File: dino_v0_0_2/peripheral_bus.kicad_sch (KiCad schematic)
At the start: 9 parts, among them J1 DINO_BUS_SOCKET, J2 DINO_BUS_SOCKET, J3 DINO_BUS_SOCKET, J4 DINO_BUS_SOCKET, J5 DINO_BUS_SOCKET, J6 DINO_BUS_SOCKET, J7 DINO_BUS_SOCKET, J8 DINO_BUS_SOCKET, U78 74LS04

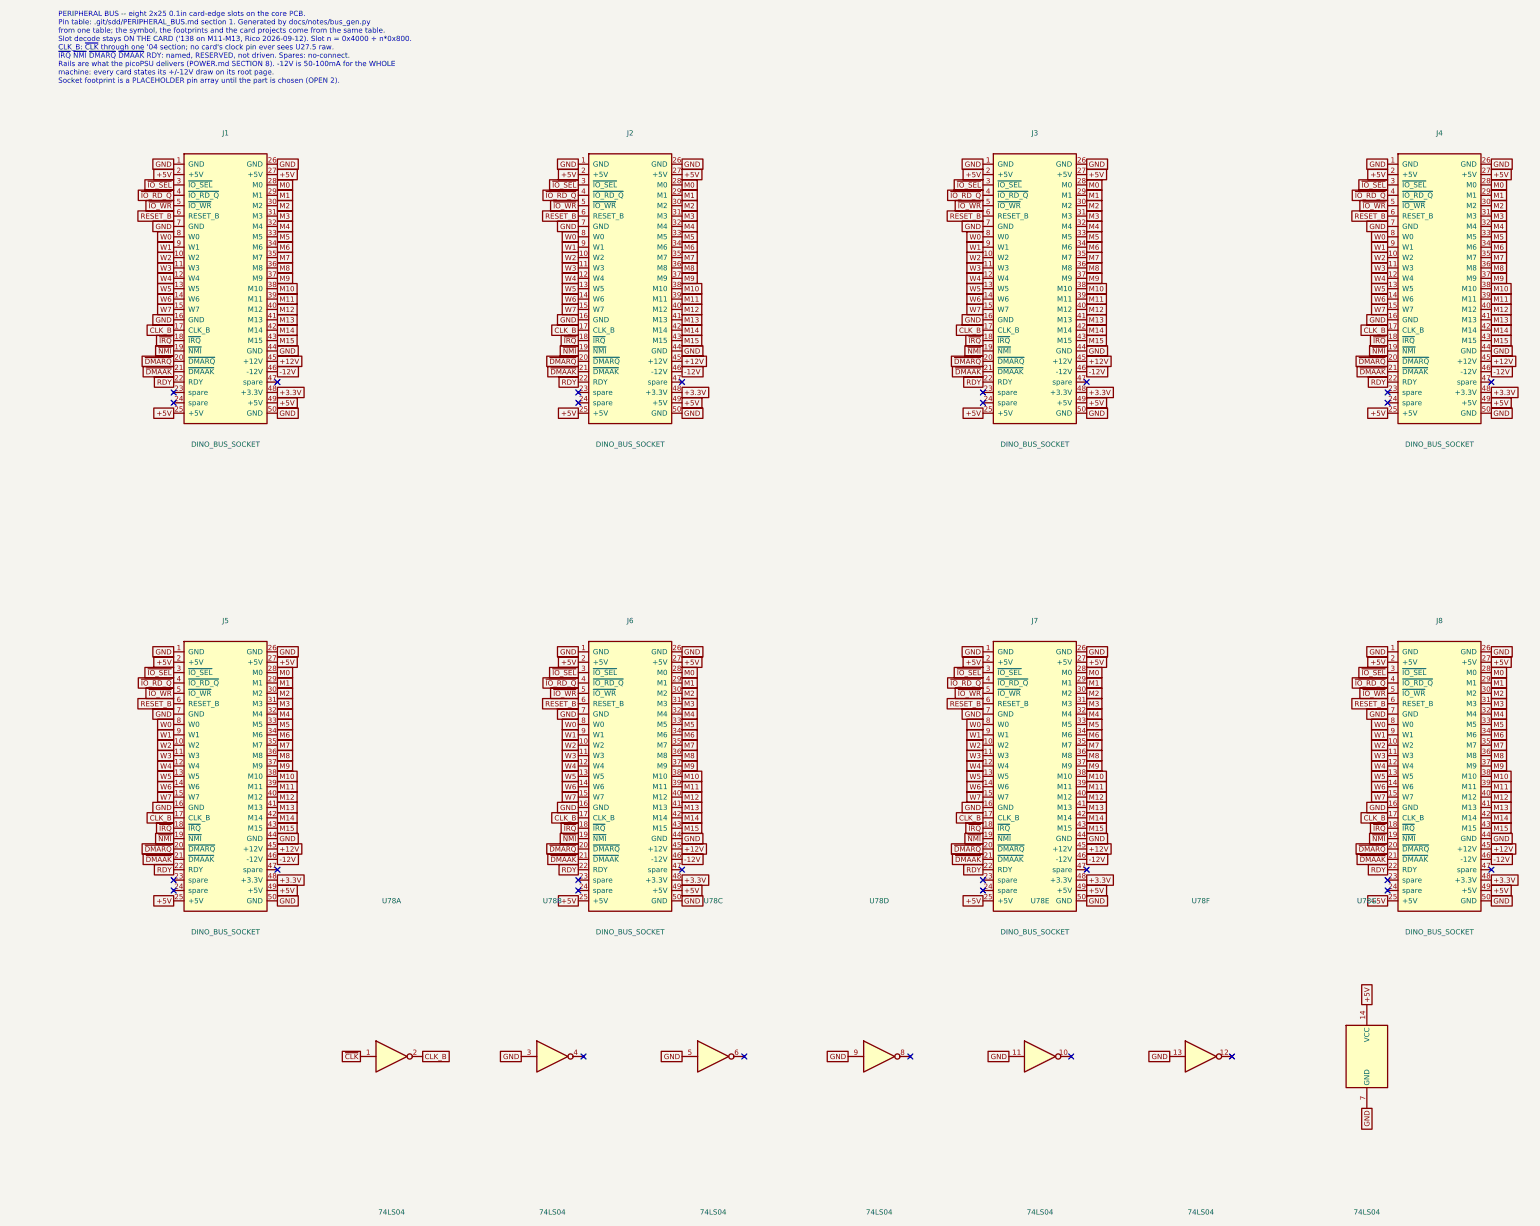
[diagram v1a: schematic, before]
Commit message: feat(int): draw the interrupt block; sheet cleanup pass
New sheet dino_v0_0_2/interrupt.kicad_sch (page 15): U80-U87, R28 4.7k
pull-up on ~{IRQ}, R29 100R on the block's CLK branch, C83-C90. Every
pin per PHASE_INT SECTION 3, checked against the plan with kicad_netlist
and kicad-cli (146 pins, 0 mismatches).

Old sheets (SECTION 3.2): U28.4 lifted off GND to INJECT; U61.3 to
END_OR_ACCEPT; U36.1 to PC_UP_GATED; U49 D0-3 cut from U48 Za-Zd and
routed through U87 as FLAG_NEXT0-3 / FLAG_D0-3; FLAG_C/Z/V/N and the
five decoder outputs made global. dino_serial: U104 74LS05, INTR ->
~{IRQ}, C4.

Placement pass on every sheet: bus entries and global labels no longer
share wires; M, CW, T, IRB and SA buses kept as labelled keys. Nets
diffed against HEAD per sheet: only the intended changes and a rotated
C29. Project ERC: 0 errors. MODULE CONTRACT stamps regenerated.

Co-Authored-By: Claude Fable 5.1 <noreply@anthropic.com>
Claude-Session: https://claude.ai/code/session_01JGxSS4MVUcaZdKZGtKroSg
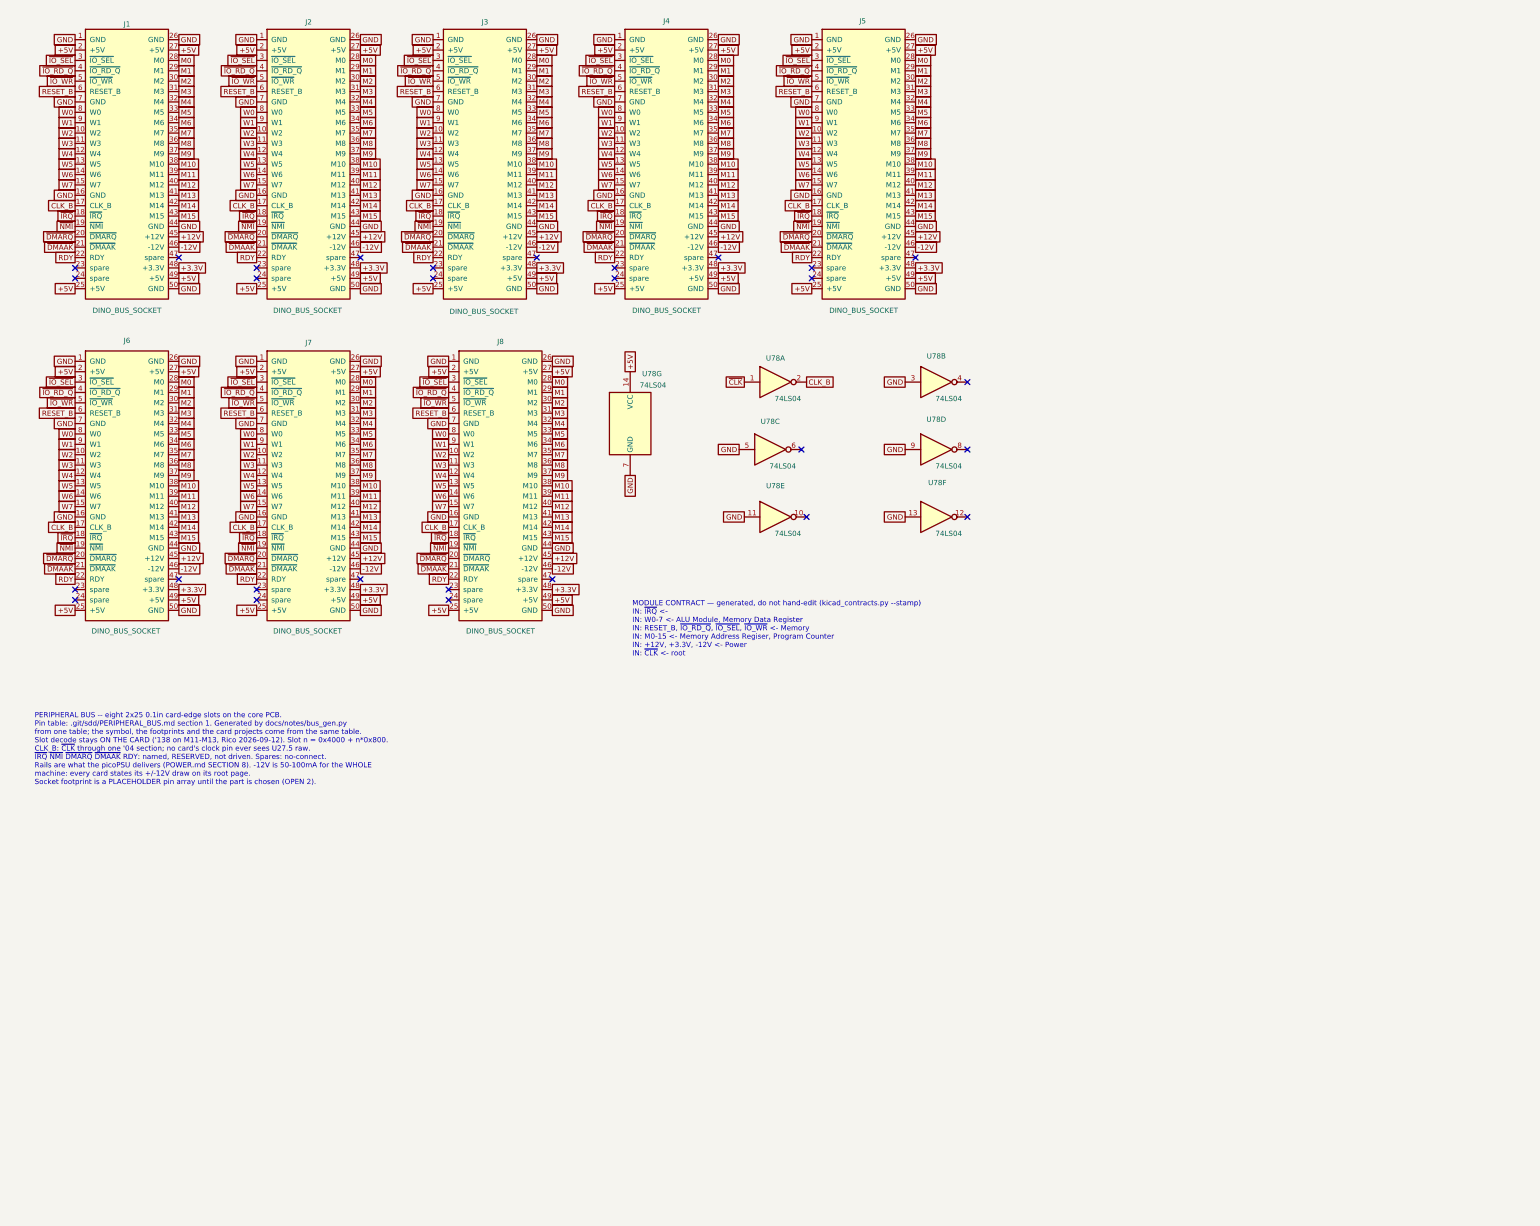
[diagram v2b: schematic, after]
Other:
- note added: "MODULE CONTRACT — generated, do not hand-edit (kicad_contracts.py --stamp) IN: ~{IRQ} <- IN: W0-7 <- ALU Module, Memory Data Register IN: RESET_B, ~{IO_RD_Q}, ~{IO_SEL}, ~{IO_WR} <- Memory IN: M0-15 <- Memory Address Regiser, Program Counter IN: +12V, +3.3V, -12V <- Power IN: ~{CLK} <- root"
- moved on the sheet: J1, J2, J3, J4, J5, J6, J7, J8, U78A, U78B, U78C, U78D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

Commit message: feat(pcb): sync board to schematic; fuse, bulk caps, RDY pull-up
Update PCB from schematic: the INT block (U80-U87), U76, the four
copper fixes (WR_GATE, CLK_ALU, INJECT, PC_UP gate) and the renumbered
W pull-ups (R9-R13, R30-R32 replace R4-R8, R25-R27). DRC schematic
parity 0.

Power: an old ATX tower supply into J9. +5V enters through F1 (3A
slow-blow, 5x20), J9's 5V pins on +5V_IN; C91 470uF + C92 10uF bulk;
PWR_FLAG on +5V. R33 10k pull-up on RDY. ERC unchanged from the
2026-10-06 baseline. Fix duplicate #PWR158 on the interrupt sheet.

Co-Authored-By: Claude Opus 5.5 <noreply@anthropic.com>
Claude-Session: https://claude.ai/code/session_01JGxSS4MVUcaZdKZGtKroSg
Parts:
- added R33: 10kΩ, Resistor_THT:R_Axial_DIN0207_L6.3mm_D2.5mm_P10.16mm_Horizontal, symbol Device:R
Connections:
- net +5V: now also R33.1
- net RDY: now also R33.2

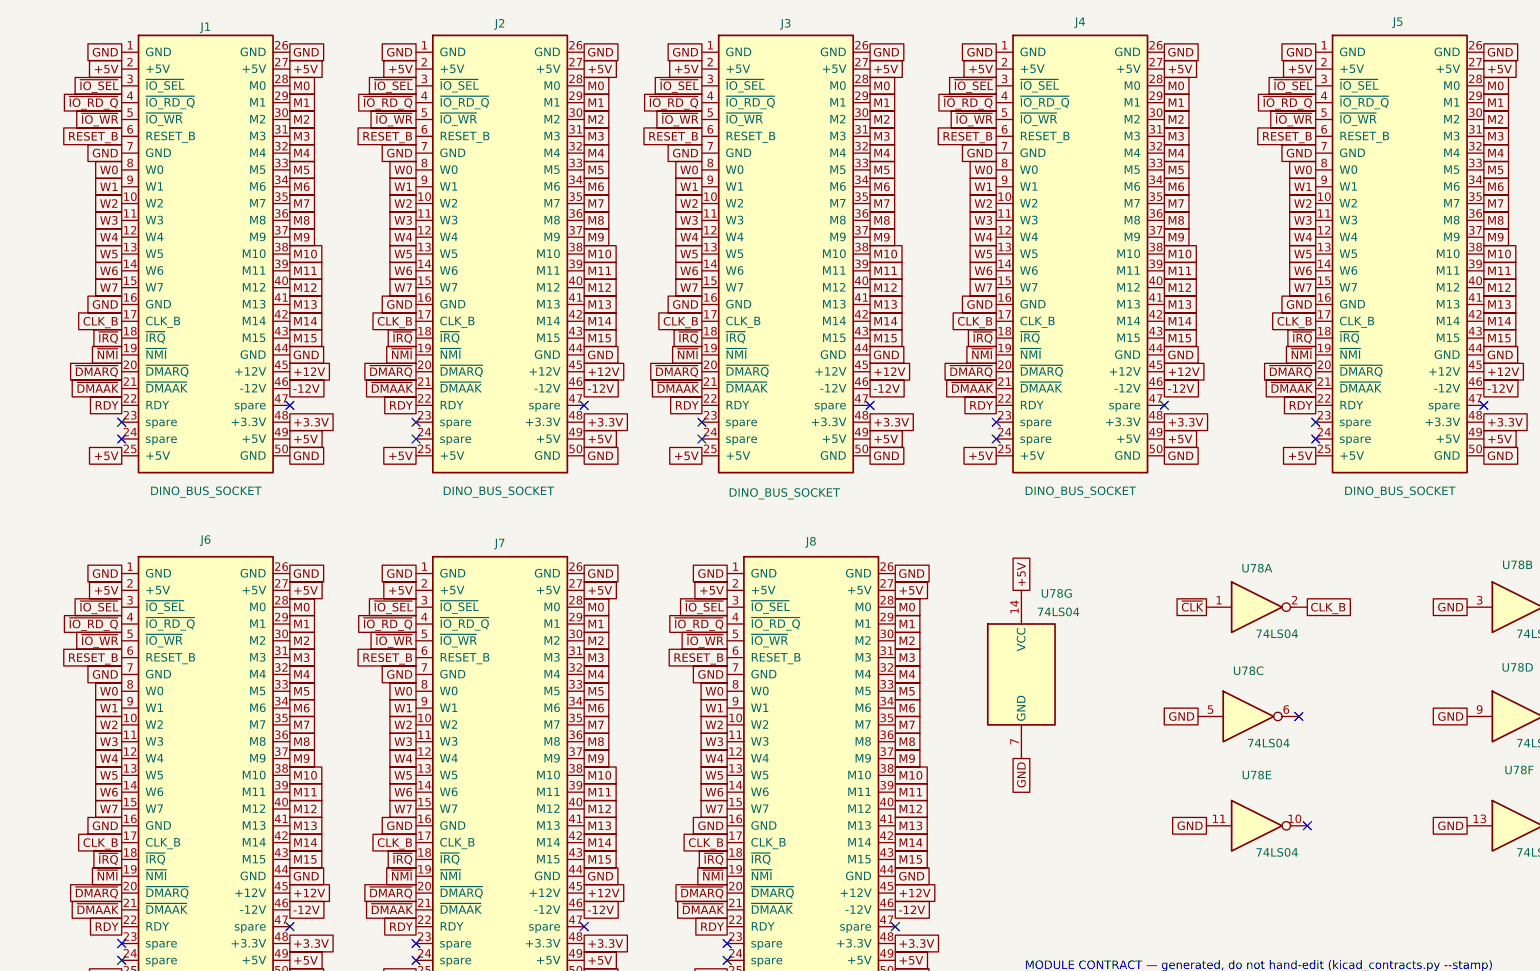
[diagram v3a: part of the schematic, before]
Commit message: feat(pcb): Rev A fab gate, CLK_B to edge pin 1, re-routed DRC clean
Fab gate S4: CLKIN header J13 + JP3 (Y1 / external clock select),
R34 100R in series on CLK_B, Sullins EBC25DCWN footprints on J1-J8.

CLK_B moves from edge pin 17 to pin 1 (pin 17 becomes GND). From
mid-row pin 17 every slot-to-slot run had to go round the other row's
end: 0.84 mm between socket pads is less than the CLK class needs
(0.3 mm + 2 x 0.4 mm), so it routed to 503-517 mm. From pin 1 it runs
straight down the slot column: 164 mm, with +5V beside it and GND
across. Source termination (R34) only holds on an electrically short
line (Philips AN246). bus_gen.py, the dino_bus symbol, the schematic
and the board all move together; no card exists yet.

Routed by Freerouting 2.5.0 (JDK 25) from an empty board; 2.1.0
headless never joins two neighbouring pins on one net. Default
netclass 0.2/0.15 mm, RESET clearance 0.6 mm. Silkscreen cleaned up.
KiCad DRC: 0 unconnected, 0 errors, schematic parity 0; one
text_thickness warning on the TrueType board text. ERC at its baseline
(74). test_pcb_envelope 7/7, including the new RESET adjacency test.
Fab zip: fabrication/dino_rev_a_gerbers_20261029_0756.zip.

Co-Authored-By: Claude Opus 5.5 <noreply@anthropic.com>
Claude-Session: https://claude.ai/code/session_01JGxSS4MVUcaZdKZGtKroSg
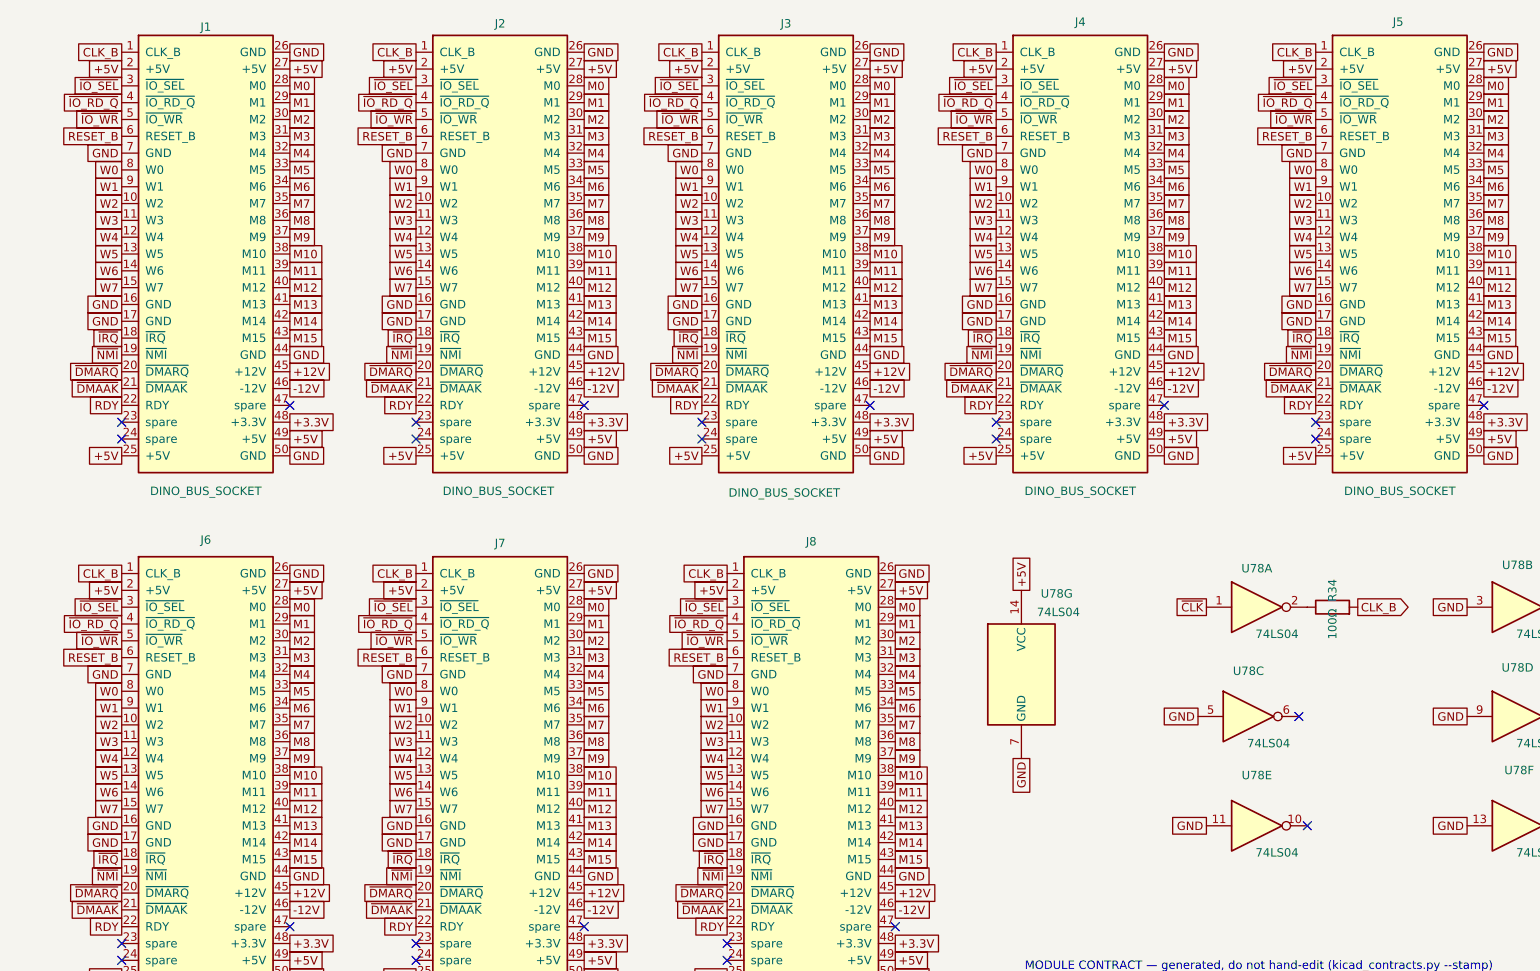
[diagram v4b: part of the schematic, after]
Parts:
- added R34: 100Ω, Resistor_THT:R_Axial_DIN0207_L6.3mm_D2.5mm_P10.16mm_Horizontal, symbol Device:R
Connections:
- net CLK_B: now also J1.1 (CLK_B), J2.1 (CLK_B), J3.1 (CLK_B), J4.1 (CLK_B), J5.1 (CLK_B), J6.1 (CLK_B), J7.1 (CLK_B), J8.1 (CLK_B), R34.2; no longer J1.17 (CLK_B), J2.17 (CLK_B), J3.17 (CLK_B), J4.17 (CLK_B), J5.17 (CLK_B), J6.17 (CLK_B), J7.17 (CLK_B), J8.17 (CLK_B), U78.2
- net GND: now also J1.17 (GND), J2.17 (GND), J3.17 (GND), J4.17 (GND), J5.17 (GND), J6.17 (GND), J7.17 (GND), J8.17 (GND); no longer J1.1 (GND), J2.1 (GND), J3.1 (GND), J4.1 (GND), J5.1 (GND), J6.1 (GND), J7.1 (GND), J8.1 (GND)
- new net: R34.1, U78.2
